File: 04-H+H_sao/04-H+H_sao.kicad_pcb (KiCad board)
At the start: 2 copper layers, 99.2 x 90.6 mm, 15 parts, among them U1 ICM7555, X1 Badgelife_sao_connector_v169b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

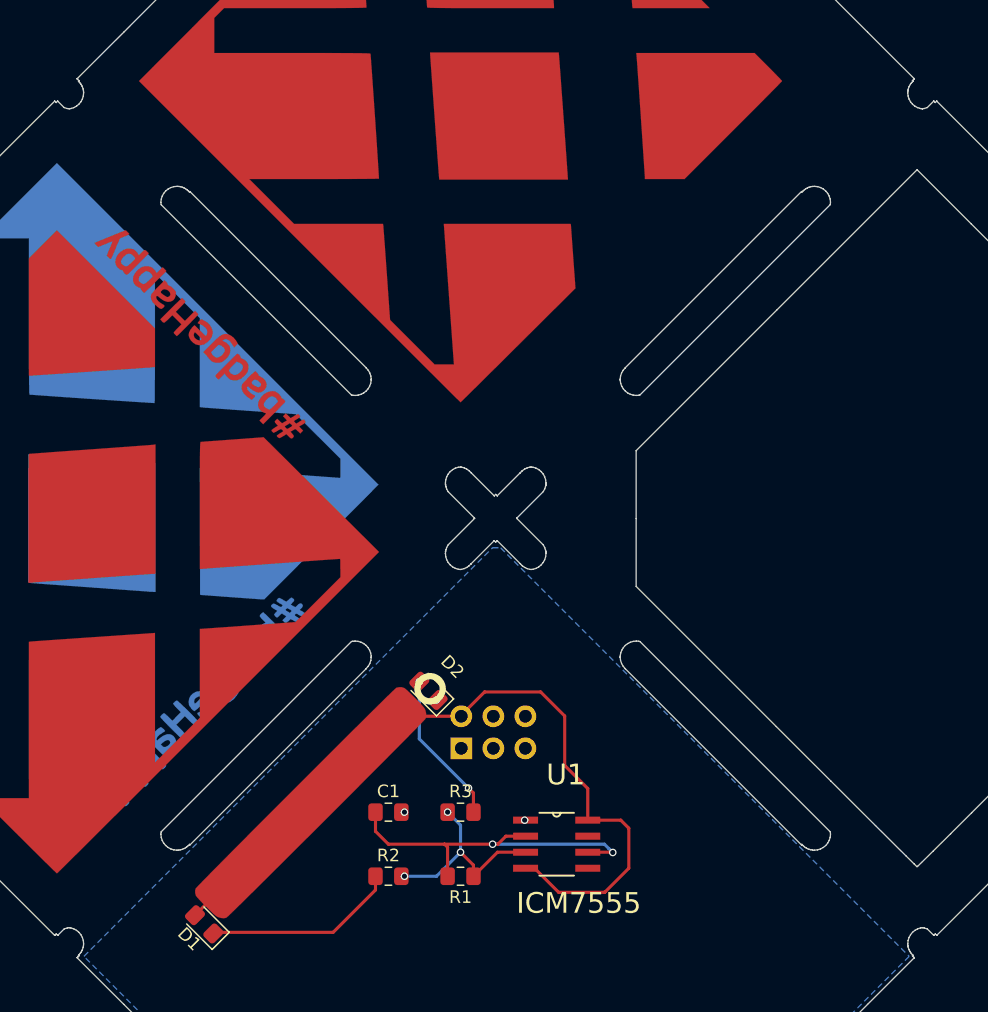
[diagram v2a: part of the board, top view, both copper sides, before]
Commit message: adding mounting hole connectors
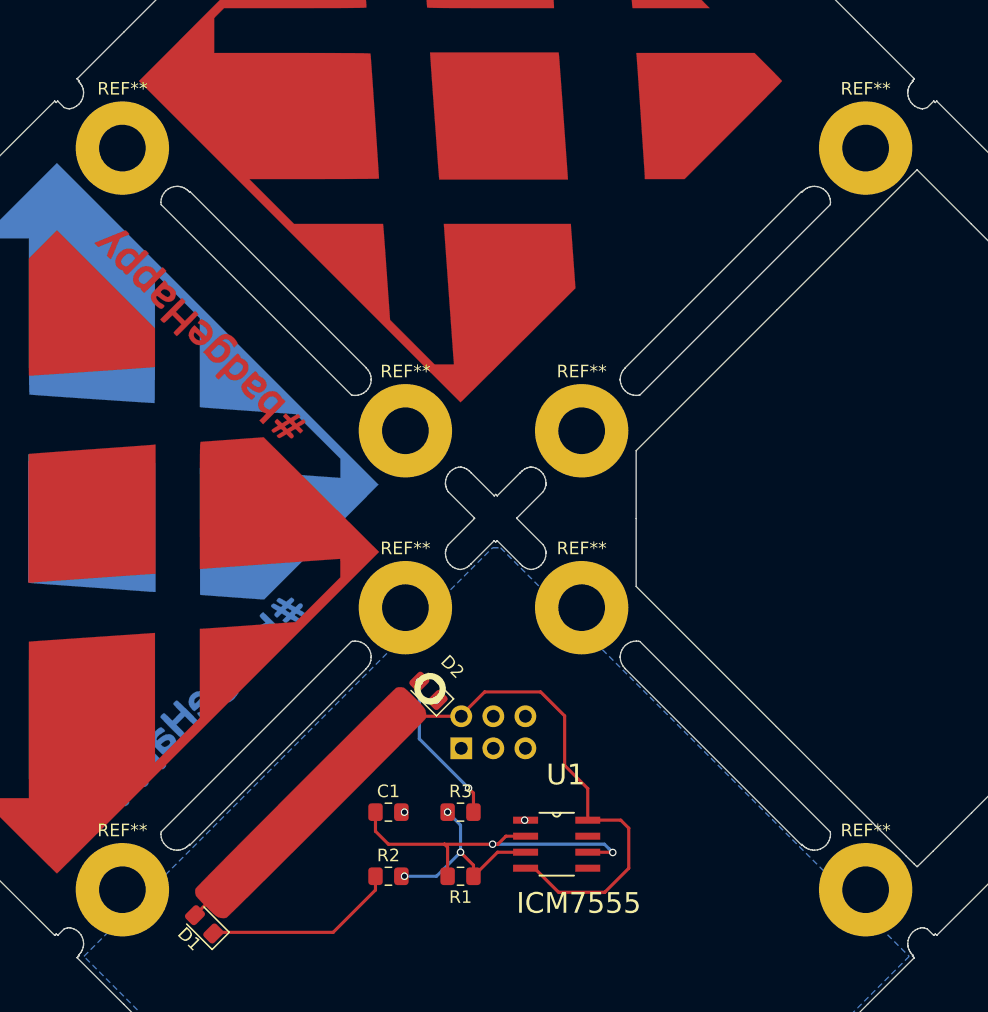
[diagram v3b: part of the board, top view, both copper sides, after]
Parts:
- removed the G*** at (146.2, 101.8) (x5)
- added G*** (x5): LOGO, LOGO, F.Cu at (146.2, 101.8)
- added REF**: MountingHole_3.7mm_Pad, MountingHole:MountingHole_3.7mm_Pad, F.Cu at (139.1, 94.9)
- added REF**: MountingHole_3.7mm_Pad, MountingHole:MountingHole_3.7mm_Pad, F.Cu at (116.7, 72.5)
- added REF**: MountingHole_3.7mm_Pad, MountingHole:MountingHole_3.7mm_Pad, F.Cu at (175.6, 72.5)
- added REF**: MountingHole_3.7mm_Pad, MountingHole:MountingHole_3.7mm_Pad, F.Cu at (175.6, 131.2)
- added REF**: MountingHole_3.7mm_Pad, MountingHole:MountingHole_3.7mm_Pad, F.Cu at (153.1, 108.9)
- added REF**: MountingHole_3.7mm_Pad, MountingHole:MountingHole_3.7mm_Pad, F.Cu at (153.1, 94.9)
- added REF**: MountingHole_3.7mm_Pad, MountingHole:MountingHole_3.7mm_Pad, F.Cu at (139.1, 108.9)
- added REF**: MountingHole_3.7mm_Pad, MountingHole:MountingHole_3.7mm_Pad, F.Cu at (116.7, 131.2)
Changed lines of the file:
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@@
     (tracks 57)
     (zones 0)
-    (modules 15)
+    (modules 23)
     (nets 13)
   )
@@
     (add_net VDD)
   )
+  (module MountingHole:MountingHole_3.7mm_Pad (layer F.Cu)
+    (at 139.1412 94.869)
+    (descr "Mounting Hole 3.7mm")
+    (tags "mounting hole 3.7mm")
+    (attr virtual)
+    (fp_text reference REF** (at 0 -4.7) (layer F.SilkS)
+      (effects (font (size 1 1) (thickness 0.15)))
+    )
+    (fp_text value MountingHole_3.7mm_Pad (at 0 4.7) (layer F.Fab)
+      (effects (font (size 1 1) (thickness 0.15)))
+    )
+    (fp_text user %R (at 0.3 0) (layer F.Fab)
+      (effects (font (size 1 1) (thickness 0.15)))
+    )
+    (fp_circle (center 0 0) (end 3.7 0) (layer Cmts.User) (width 0.15))
+    (fp_circle (center 0 0) (end 3.95 0) (layer F.CrtYd) (width 0.05))
+    (pad 1 thru_hole circle (at 0 0) (size 7.4 7.4) (drill 3.7) (layers *.Cu *.Mask))
+  )
+  (module MountingHole:MountingHole_3.7mm_Pad (layer F.Cu)
+    (at 116.713 72.4662)
+    (descr "Mounting Hole 3.7mm")
+    (tags "mounting hole 3.7mm")
+    (attr virtual)
+    (fp_text reference REF** (at 0 -4.7) (layer F.SilkS)
+      (effects (font (size 1 1) (thickness 0.15)))
+    )
+    (fp_text value MountingHole_3.7mm_Pad (at 0 4.7) (layer F.Fab)
+      (effects (font (size 1 1) (thickness 0.15)))
+    )
+    (fp_circle (center 0 0) (end 3.95 0) (layer F.CrtYd) (width 0.05))
+    (fp_circle (center 0 0) (end 3.7 0) (layer Cmts.User) (width 0.15))
+    (fp_text user %R (at 0.3 0) (layer F.Fab)
+      (effects (font (size 1 1) (thickness 0.15)))
+    )
+    (pad 1 thru_hole circle (at 0 0) (size 7.4 7.4) (drill 3.7) (layers *.Cu *.Mask))
+  )
+  (module MountingHole:MountingHole_3.7mm_Pad (layer F.Cu)
+    (at 175.6156 72.4662)
+    (descr "Mounting Hole 3.7mm")
+    (tags "mounting hole 3.7mm")
+    (attr virtual)
+    (fp_text reference REF** (at 0 -4.7) (layer F.SilkS)
+      (effects (font (size 1 1) (thickness 0.15)))
+    )
+    (fp_text value MountingHole_3.7mm_Pad (at 0 4.7) (layer F.Fab)
+      (effects (font (size 1 1) (thickness 0.15)))
+    )
+    (fp_text user %R (at 0.3 0) (layer F.Fab)
+      (effects (font (size 1 1) (thickness 0.15)))
+    )
+    (fp_circle (center 0 0) (end 3.7 0) (layer Cmts.User) (width 0.15))
+    (fp_circle (center 0 0) (end 3.95 0) (layer F.CrtYd) (width 0.05))
+    (pad 1 thru_hole circle (at 0 0) (size 7.4 7.4) (drill 3.7) (layers *.Cu *.Mask))
+  )
+  (module MountingHole:MountingHole_3.7mm_Pad (layer F.Cu)
+    (at 175.6156 131.2418)
+    (descr "Mounting Hole 3.7mm")
+    (tags "mounting hole 3.7mm")
+    (attr virtual)
+    (fp_text reference REF** (at 0 -4.7) (layer F.SilkS)
+      (effects (font (size 1 1) (thickness 0.15)))
+    )
+    (fp_text value MountingHole_3.7mm_Pad (at 0 4.7) (layer F.Fab)
+      (effects (font (size 1 1) (thickness 0.15)))
+    )
+    (fp_circle (center 0 0) (end 3.95 0) (layer F.CrtYd) (width 0.05))
+    (fp_circle (center 0 0) (end 3.7 0) (layer Cmts.User) (width 0.15))
+    (fp_text user %R (at 0.3 0) (layer F.Fab)
+      (effects (font (size 1 1) (thickness 0.15)))
+    )
+    (pad 1 thru_hole circle (at 0 0) (size 7.4 7.4) (drill 3.7) (layers *.Cu *.Mask))
+  )
+  (module MountingHole:MountingHole_3.7mm_Pad (layer F.Cu)
+    (at 153.1112 108.8898)
+    (descr "Mounting Hole 3.7mm")
+    (tags "mounting hole 3.7mm")
+    (attr virtual)
+    (fp_text reference REF** (at 0 -4.7) (layer F.SilkS)
+      (effects (font (size 1 1) (thickness 0.15)))
+    )
+    (fp_text value MountingHole_3.7mm_Pad (at 0 4.7) (layer F.Fab)
+      (effects (font (size 1 1) (thickness 0.15)))
+    )
+    (fp_text user %R (at 0.3 0) (layer F.Fab)
+      (effects (font (size 1 1) (thickness 0.15)))
+    )
+    (fp_circle (center 0 0) (end 3.7 0) (layer Cmts.User) (width 0.15))
+    (fp_circle (center 0 0) (end 3.95 0) (layer F.CrtYd) (width 0.05))
+    (pad 1 thru_hole circle (at 0 0) (size 7.4 7.4) (drill 3.7) (layers *.Cu *.Mask))
+  )
+  (module MountingHole:MountingHole_3.7mm_Pad (layer F.Cu)
+    (at 153.1112 94.869)
+    (descr "Mounting Hole 3.7mm")
+    (tags "mounting hole 3.7mm")
+    (attr virtual)
+    (fp_text reference REF** (at 0 -4.7) (layer F.SilkS)
+      (effects (font (size 1 1) (thickness 0.15)))
+    )
+    (fp_text value MountingHole_3.7mm_Pad (at 0 4.7) (layer F.Fab)
+      (effects (font (size 1 1) (thickness 0.15)))
+    )
+    (fp_circle (center 0 0) (end 3.95 0) (layer F.CrtYd) (width 0.05))
+    (fp_circle (center 0 0) (end 3.7 0) (layer Cmts.User) (width 0.15))
+    (fp_text user %R (at 0.3 0) (layer F.Fab)
+      (effects (font (size 1 1) (thickness 0.15)))
+    )
+    (pad 1 thru_hole circle (at 0 0) (size 7.4 7.4) (drill 3.7) (layers *.Cu *.Mask))
+  )
+  (module MountingHole:MountingHole_3.7mm_Pad (layer F.Cu)
+    (at 139.1412 108.8898)
+    (descr "Mounting Hole 3.7mm")
+    (tags "mounting hole 3.7mm")
+    (attr virtual)
+    (fp_text reference REF** (at 0 -4.7) (layer F.SilkS)
+      (effects (font (size 1 1) (thickness 0.15)))
+    )
+    (fp_text value MountingHole_3.7mm_Pad (at 0 4.7) (layer F.Fab)
+      (effects (font (size 1 1) (thickness 0.15)))
+    )
+    (fp_text user %R (at 0.3 0) (layer F.Fab)
+      (effects (font (size 1 1) (thickness 0.15)))
+    )
+    (fp_circle (center 0 0) (end 3.7 0) (layer Cmts.User) (width 0.15))
+    (fp_circle (center 0 0) (end 3.95 0) (layer F.CrtYd) (width 0.05))
+    (pad 1 thru_hole circle (at 0 0) (size 7.4 7.4) (drill 3.7) (layers *.Cu *.Mask))
+  )
   (module 04-H+H_sao:Badgelife-SAOv169-SAO-2x3 (layer F.Cu)
     (at 146.05 118.745)
@@
       (net 4 VDD))
   )
+  (module MountingHole:MountingHole_3.7mm_Pad (layer F.Cu)
+    (at 116.713 131.2418)
+    (descr "Mounting Hole 3.7mm")
+    (tags "mounting hole 3.7mm")
+    (attr virtual)
+    (fp_text reference REF** (at 0 -4.7) (layer F.SilkS)
+      (effects (font (size 1 1) (thickness 0.15)))
+    )
+    (fp_text value MountingHole_3.7mm_Pad (at 0 4.7) (layer F.Fab)
+      (effects (font (size 1 1) (thickness 0.15)))
+    )
+    (fp_circle (center 0 0) (end 3.95 0) (layer F.CrtYd) (width 0.05))
+    (fp_circle (center 0 0) (end 3.7 0) (layer Cmts.User) (width 0.15))
+    (fp_text user %R (at 0.3 0) (layer F.Fab)
+      (effects (font (size 1 1) (thickness 0.15)))
+    )
+    (pad 1 thru_hole circle (at 0 0) (size 7.4 7.4) (drill 3.7) (layers *.Cu *.Mask))
+  )
   (gr_line (start 139.243104 56.520225) (end 139.243104 56.520741) (layer Edge.Cuts) (width 0.1))

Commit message: first prototype gerbers
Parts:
- removed the G*** at (146.2, 101.8) (x5)
- added G*** (x5): LOGO, LOGO, F.Cu at (146.2, 101.8)
- turned X1 to 180 degrees
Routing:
- net VDD: track 62.9 -> 68.8 mm

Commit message: Hth mk2 (#1)
* moving edge cuts to make front and back smaller

* adding front silk to minimize light leak through mask

* index layers for resize

* resized

* distributed layers and refill black

* generated new pcb from svg
added mouse bites and regular breakaway connectors

* placed circuit

* rotated board design to put labels upside right

* rotated board

* generated mk2 gerbers

* wip

* rotated again

* fixing board shape in svg
adding solder pads for binding layers

* final render

* fixing back copper for hashtag

* graphics cleanup

* adding solder notches

* new renders with solder notches

* removing notches and plotting Gerbers

* adding mk1 gerbers

* adding board that wont be overwritten

* final super H+H

* adding h+h board for just backs

* adding sch
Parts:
- removed ?: , Wire_Pads:SolderWirePad_single_0-8mmDrill
- removed C1: 10U, Capacitor_SMD:C_0805_2012Metric_Pad1.15x1.40mm_HandSolder
- removed D1, D2: LED, LED_SMD:LED_0805_2012Metric_Pad1.15x1.40mm_HandSolder
- removed the G*** at (146.2, 101.8) (x5)
- removed the G*** at (0.00, 0.00)
- removed R1: 110K, Resistor_SMD:R_0805_2012Metric_Pad1.15x1.40mm_HandSolder
- removed R2, R3: 110, Resistor_SMD:R_0805_2012Metric_Pad1.15x1.40mm_HandSolder
- removed REF** (x8): MountingHole_3.7mm_Pad, MountingHole:MountingHole_3.7mm_Pad
- removed U1: ICM7555, ICM7555IBAZ-T:SOIC127P600X175-8N
- removed X1: Badgelife_sao_connector_v169bis, 04-H+H_sao:Badgelife-SAOv169-SAO-2x3
- added G*** (x6): LOGO, LOGO, F.Cu at (0.00, 0.00)
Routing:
- net VDD: track 68.8 -> 0.00 mm
- net Drain: track 28.5 -> 0.00 mm, vias 2 -> 0
- net Net-(R1-Pad1): track 16.8 -> 0.00 mm, vias 3 -> 0
- net Net-(D1-Pad1): track 15.4 -> 0.00 mm
- net Net-(D2-Pad2): track 12.1 -> 0.00 mm, vias 2 -> 0
- net GND: vias 3 -> 0
- removed copper zone on B.Cu, net GND
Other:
- board size 99.2 x 90.6 mm -> 98.4 x 93.8 mm
